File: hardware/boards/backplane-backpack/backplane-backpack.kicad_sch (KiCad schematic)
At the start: 0 parts

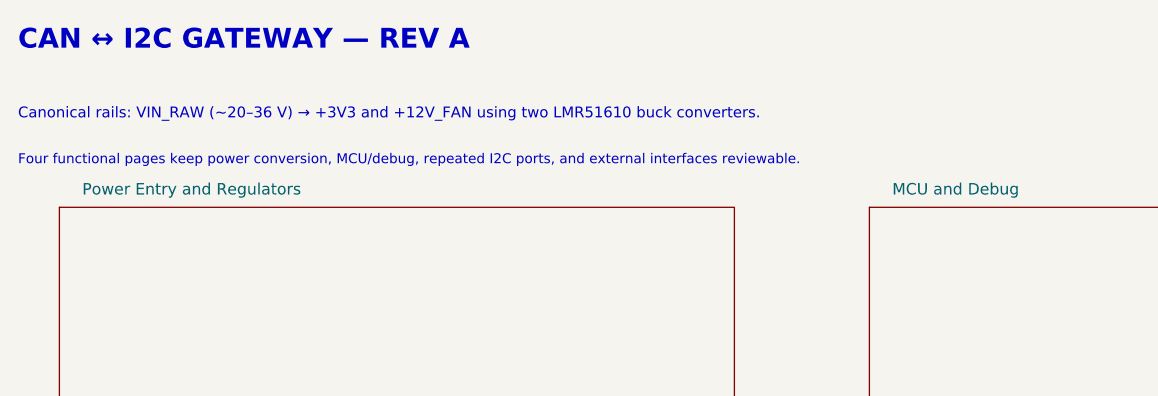
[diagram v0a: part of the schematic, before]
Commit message: fix: standardize 12V rail and mirror buck layout
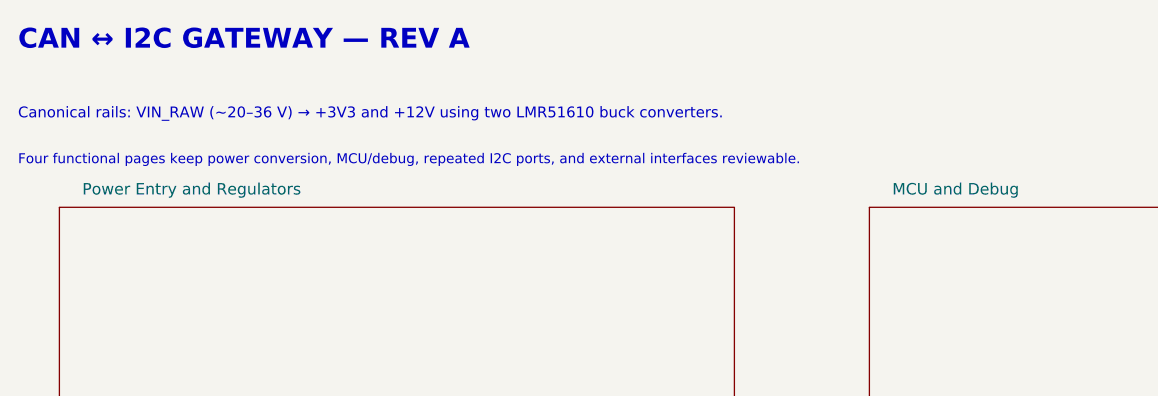
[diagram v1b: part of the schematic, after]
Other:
- note added: "Canonical rails: VIN_RAW (~20–36 V) → +3V3 and +12V using two LMR51610 buck converters."
- note removed: "Canonical rails: VIN_RAW (~20–36 V) → +3V3 and +12V_FAN using two LMR51610 buck converters."
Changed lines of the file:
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@@
 		(company "Karl Quinsland")
 	)
-	(text "Canonical rails: VIN_RAW (~20–36 V) → +3V3 and +12V_FAN using two LMR51610 buck converters."
+	(text "Canonical rails: VIN_RAW (~20–36 V) → +3V3 and +12V using two LMR51610 buck converters."
 		(exclude_from_sim no)
 		(at 25.4 25.4 0)

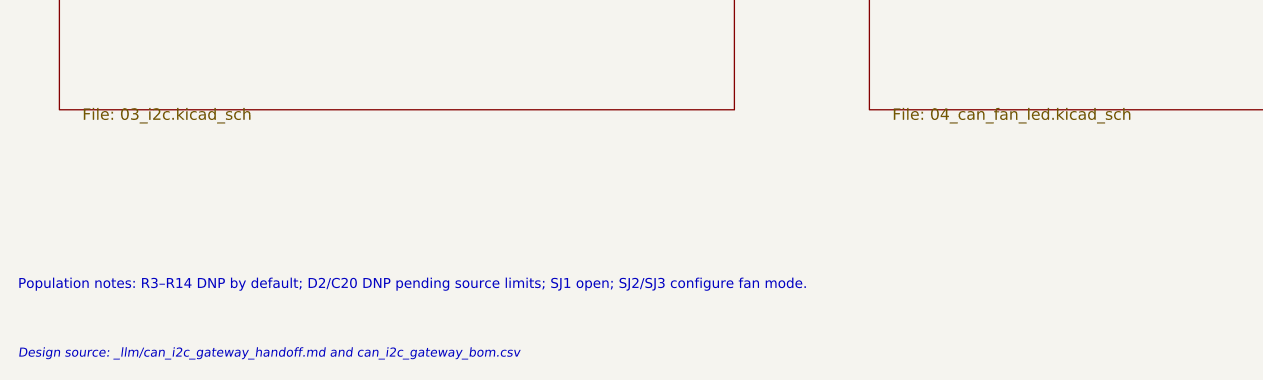
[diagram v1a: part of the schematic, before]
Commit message: refactor: move slot I2C protection to backplane
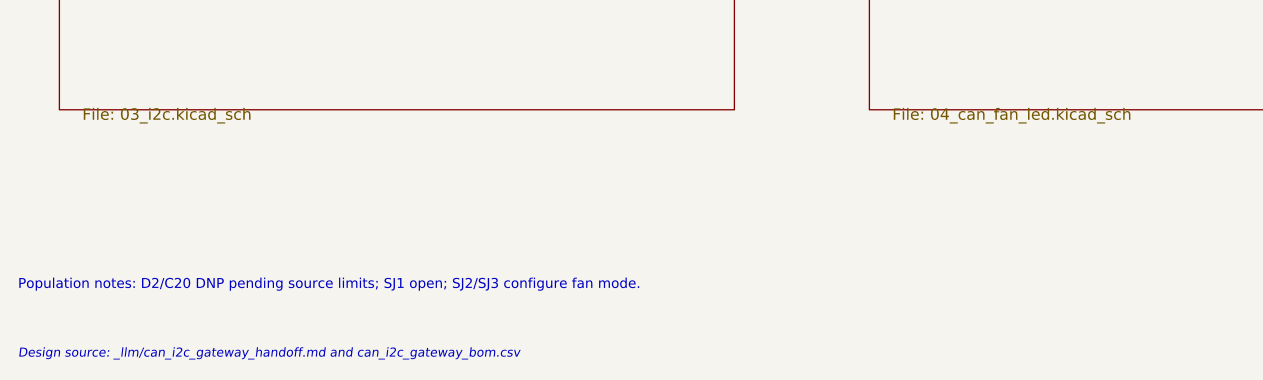
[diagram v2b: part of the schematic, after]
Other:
- note added: "Population notes: D2/C20 DNP pending source limits; SJ1 open; SJ2/SJ3 configure fan mode."
- note removed: "Population notes: R3–R14 DNP by default; D2/C20 DNP pending source limits; SJ1 open; SJ2/SJ3 configure fan mode."
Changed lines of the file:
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@@
 		)
 	)
-	(text "Population notes: R3–R14 DNP by default; D2/C20 DNP pending source limits; SJ1 open; SJ2/SJ3 configure fan mode."
+	(text "Population notes: D2/C20 DNP pending source limits; SJ1 open; SJ2/SJ3 configure fan mode."
 		(exclude_from_sim no)
 		(at 25.4 170.18 0)

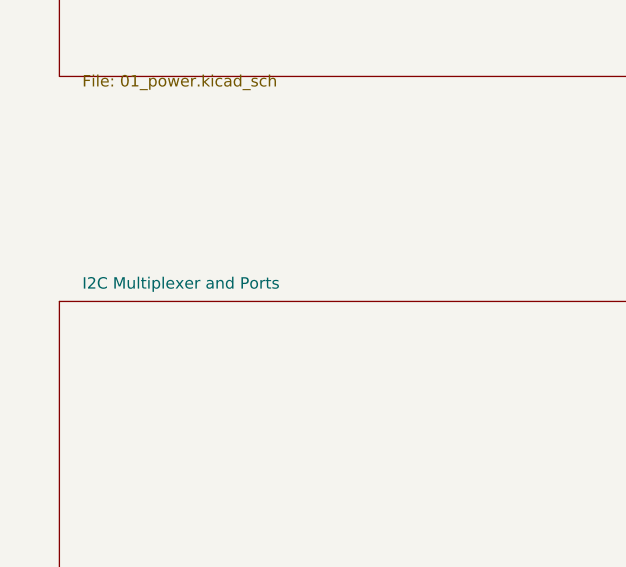
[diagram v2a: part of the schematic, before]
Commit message: Simplify backpack backplane interface
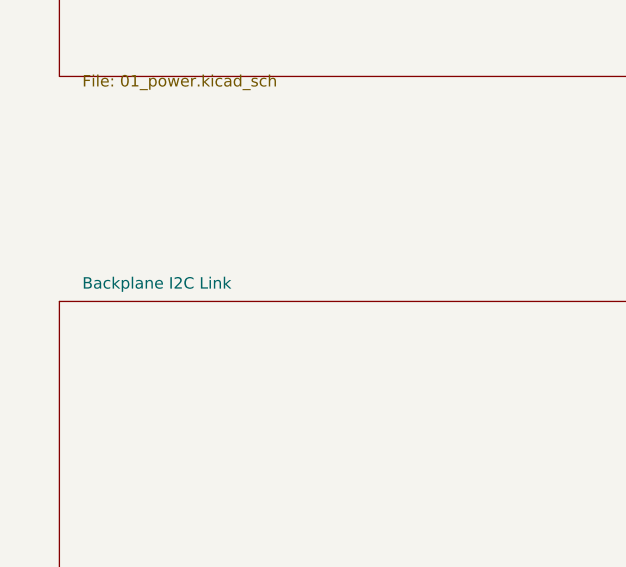
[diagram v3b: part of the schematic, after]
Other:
- sheet I2C Multiplexer and Ports renamed Backplane I2C Link
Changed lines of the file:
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@@
 			(color 0 0 0 0)
 		)
-		(property "Sheetname" "I2C Multiplexer and Ports"
+		(property "Sheetname" "Backplane I2C Link"
 			(at 32.54 103.73 0)
 			(show_name no)

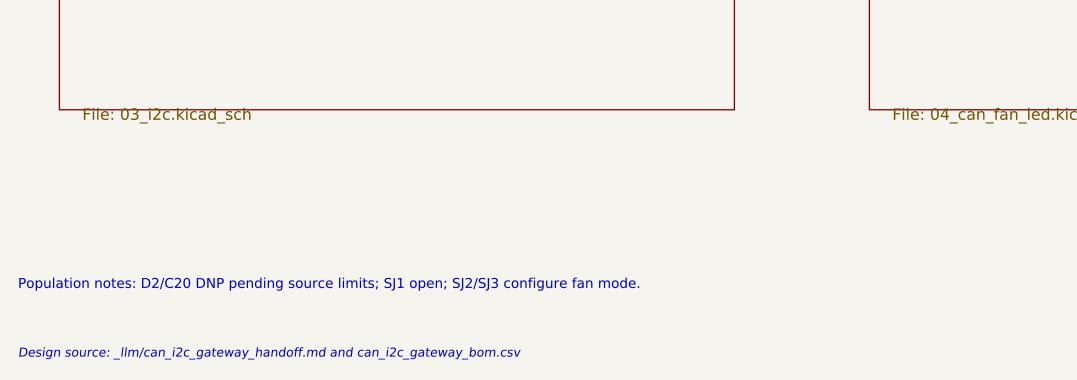
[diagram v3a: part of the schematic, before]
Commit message: hardware: simplify backpack fan interface
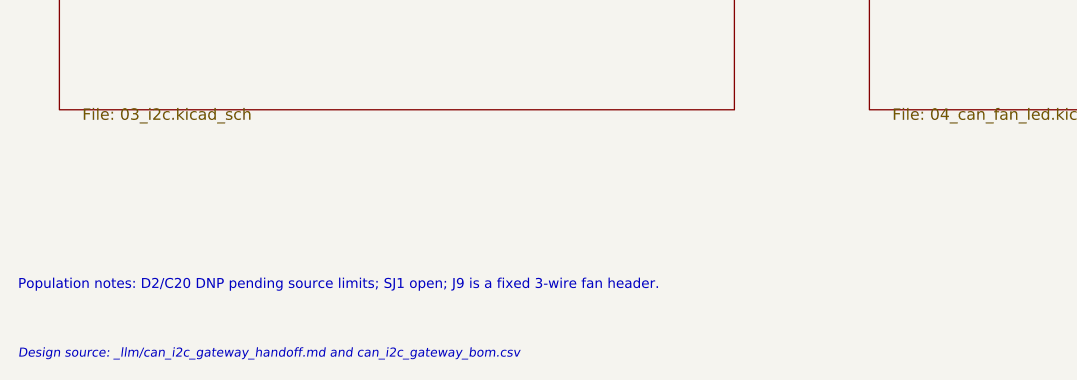
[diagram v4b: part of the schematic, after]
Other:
- note added: "Population notes: D2/C20 DNP pending source limits; SJ1 open; J9 is a fixed 3-wire fan header."
- note removed: "Population notes: D2/C20 DNP pending source limits; SJ1 open; SJ2/SJ3 configure fan mode."
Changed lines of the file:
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@@
 		)
 	)
-	(text "Population notes: D2/C20 DNP pending source limits; SJ1 open; SJ2/SJ3 configure fan mode."
+	(text "Population notes: D2/C20 DNP pending source limits; SJ1 open; J9 is a fixed 3-wire fan header."
 		(exclude_from_sim no)
 		(at 25.4 170.18 0)
